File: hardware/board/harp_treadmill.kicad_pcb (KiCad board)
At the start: 4 copper layers, 80 x 100 mm, 163 parts, among them J1 Conn_01x03_Male, J2 AudioJack3, J3 Conn_01x05_Female, J4 Conn_01x02_Female, J5 USB_C_Receptacle_USB2.0, J6 Barrel_Jack_Switch, J7 Conn_01x04_Female, Q2 Si7336ADP, U1 LP2985-3.3, U10 AD8615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

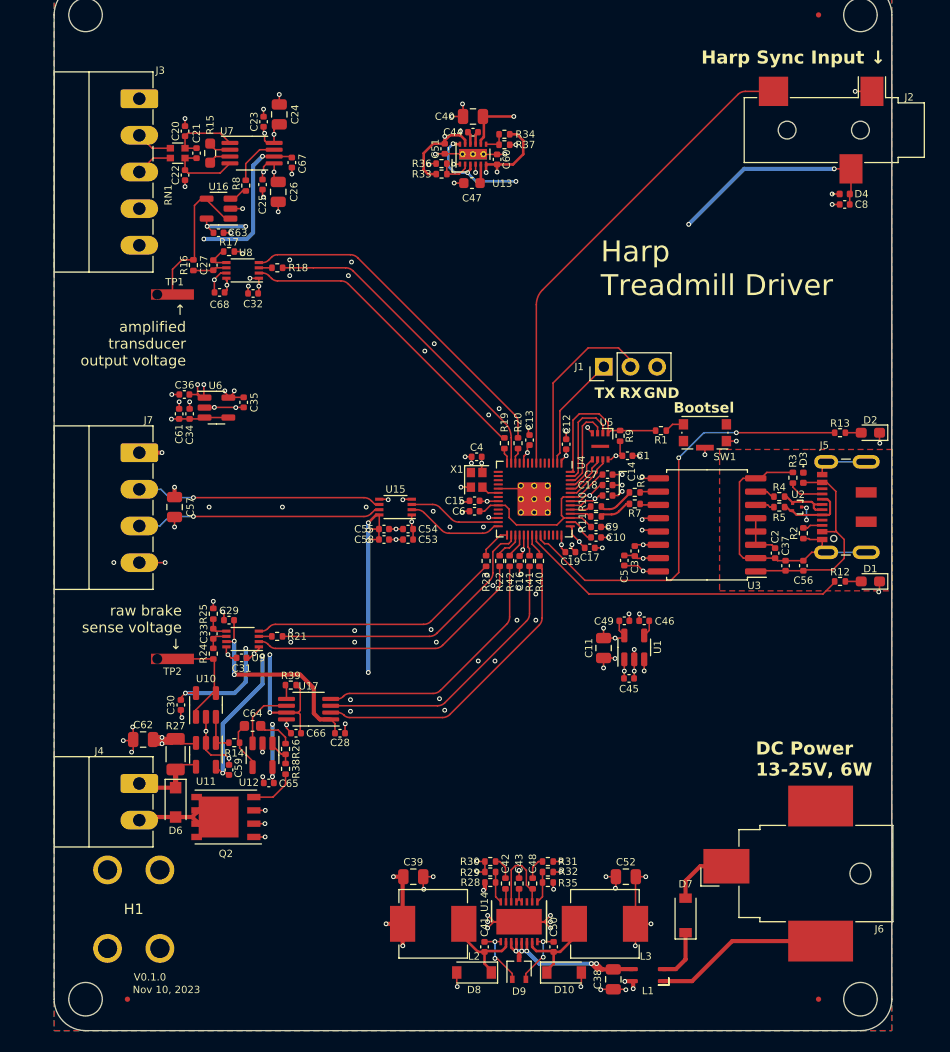
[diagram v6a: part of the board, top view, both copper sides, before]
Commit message: update pcb to v0.2.0
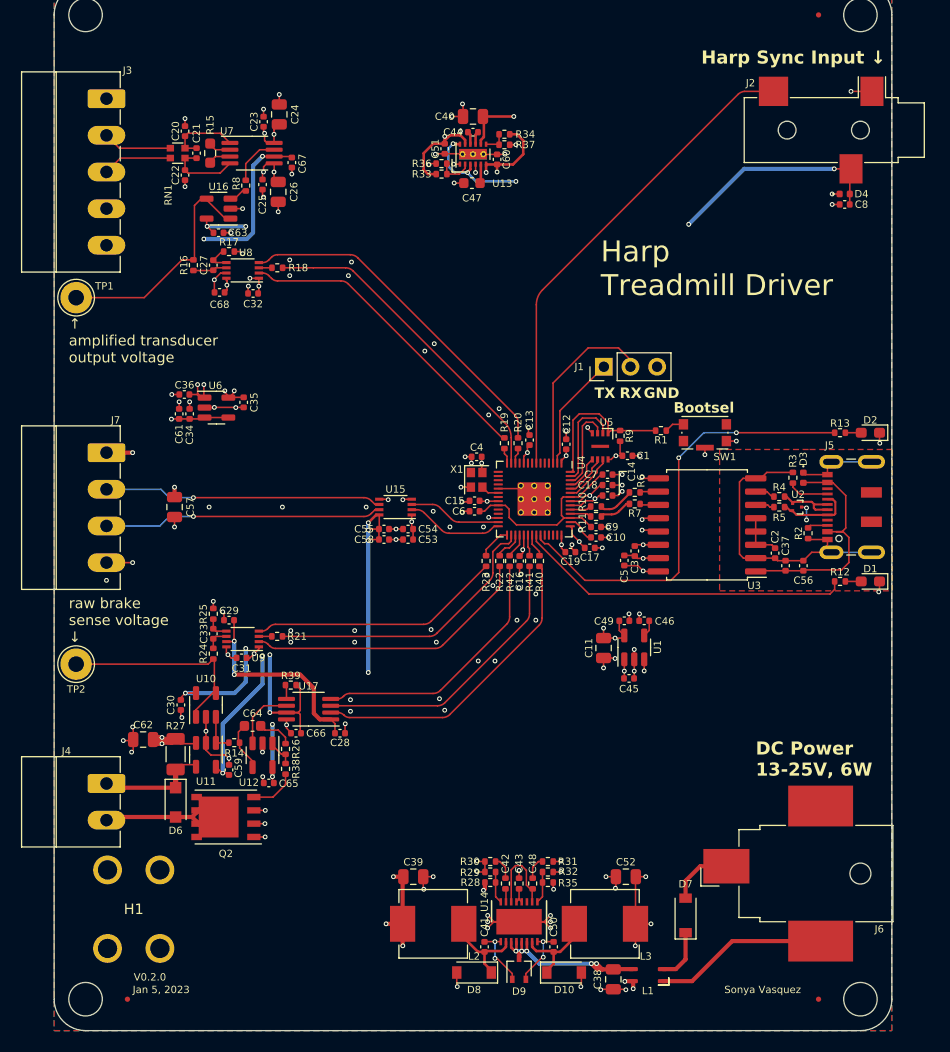
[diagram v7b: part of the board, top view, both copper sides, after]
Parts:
- TP1, TP2: footprint kicad_component_library:TestPoint_Keystone_5027_Miniature -> TestPoint:TestPoint_THTPad_D3.0mm_Drill1.5mm
- moved TP2 9.21 mm to (102.1, 95.0)
- moved TP1 9.20 mm to (102.1, 60.0)
- moved J3 3.13 mm to (105.0, 41.0)
- moved J4 3.13 mm to (105.0, 106.4)
- moved J7 3.13 mm to (105.0, 74.8)
- moved J5 0.50 mm to (176.9, 80.0)
- moved R2 0.45 mm to (172.0, 82.5)
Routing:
- net Net-(U10--): track 10.5 -> 19.9 mm
- net Net-(U16--): track 14.6 -> 22.5 mm
- net Net-(J3-Pin_3): track 3.52 -> 6.65 mm
- net Net-(D6-A): track 6.79 -> 9.92 mm
- net Net-(J7-Pin_3): track 23.5 -> 26.6 mm
- net Net-(J7-Pin_2): track 23.5 -> 26.6 mm
- net Net-(J3-Pin_2): track 3.48 -> 6.61 mm
- net Net-(D6-K): track 7.60 -> 10.7 mm
- net GND1: track 35.6 -> 38.3 mm
- net VBUS: track 20.5 -> 22.7 mm
- net /Harp Core RP2040 + Isolated USB/D+: track 5.30 -> 6.30 mm
- net Net-(J5-CC2): track 3.46 -> 3.96 mm
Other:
- board text added: "Jan 5, 2023"
- board text added: "V0.2.0"
- board text removed: "Nov 10, 2023"
- board text removed: "V0.1.0"
